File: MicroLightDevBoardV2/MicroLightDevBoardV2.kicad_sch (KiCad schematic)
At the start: 34 parts, among them J1 Conn_01x05_Socket, J10 TYPE-C-31-M-12, J11 Conn_01x04_Socket, J12 Conn_01x04_Socket, J2 Conn_01x05_Socket, J3 Conn_01x05_Socket, J4 Conn_01x05_Socket, J5 Conn_01x03_Socket, J6 Conn_01x04_Socket, J7 Conn_01x04_Socket, J8 Conn_01x05_Socket, J9 Conn_01x01_Socket, U1 BQ25628RYKR, U2 ATtiny3226-M, U3 USBLC6-2P6

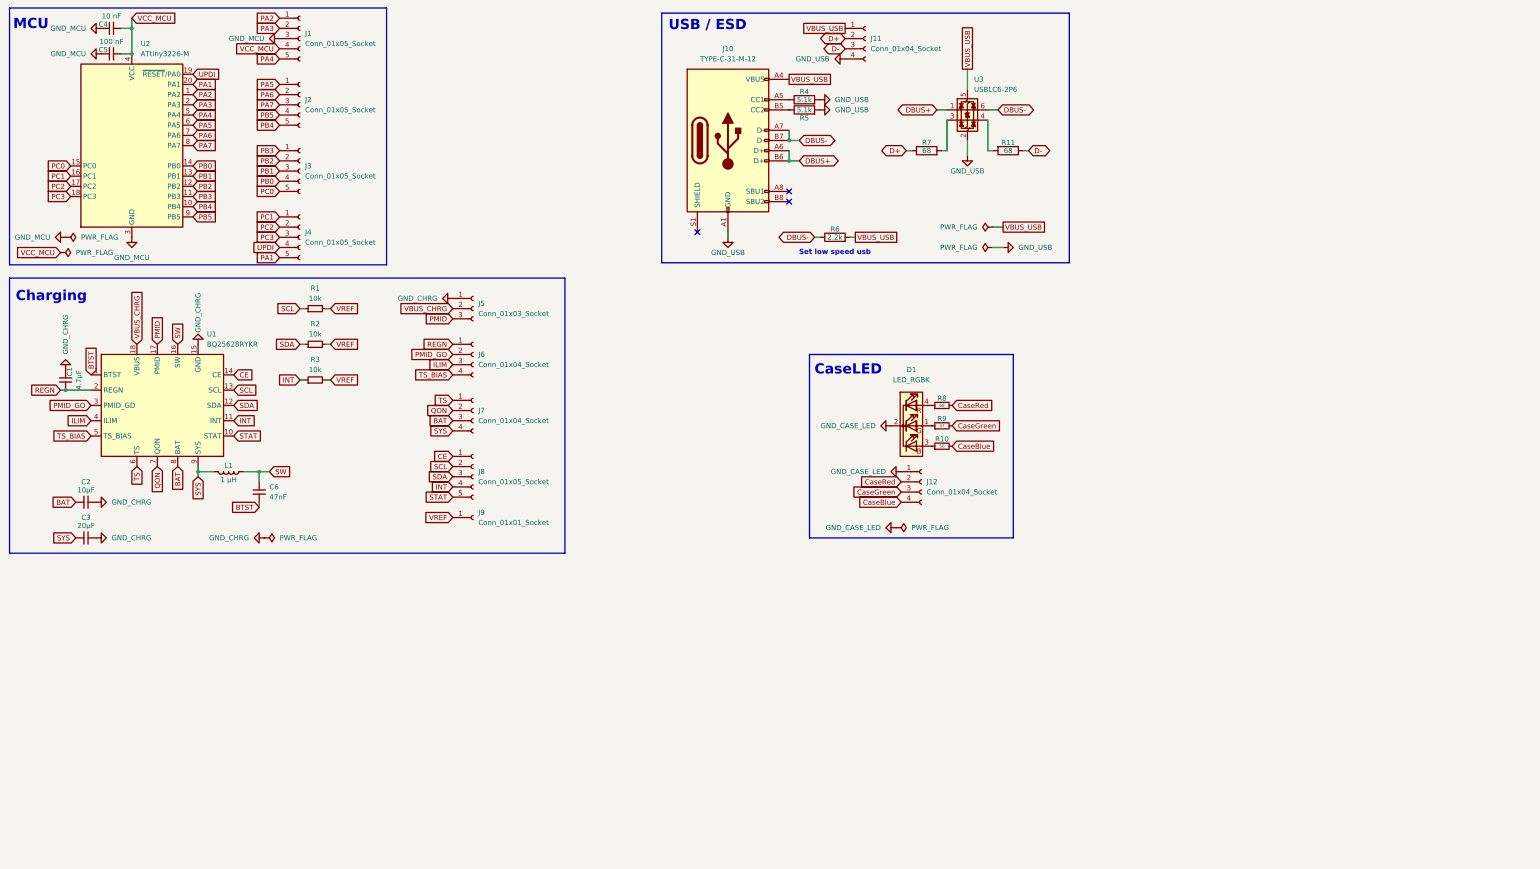
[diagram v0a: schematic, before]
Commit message: added symbol for accelerometer
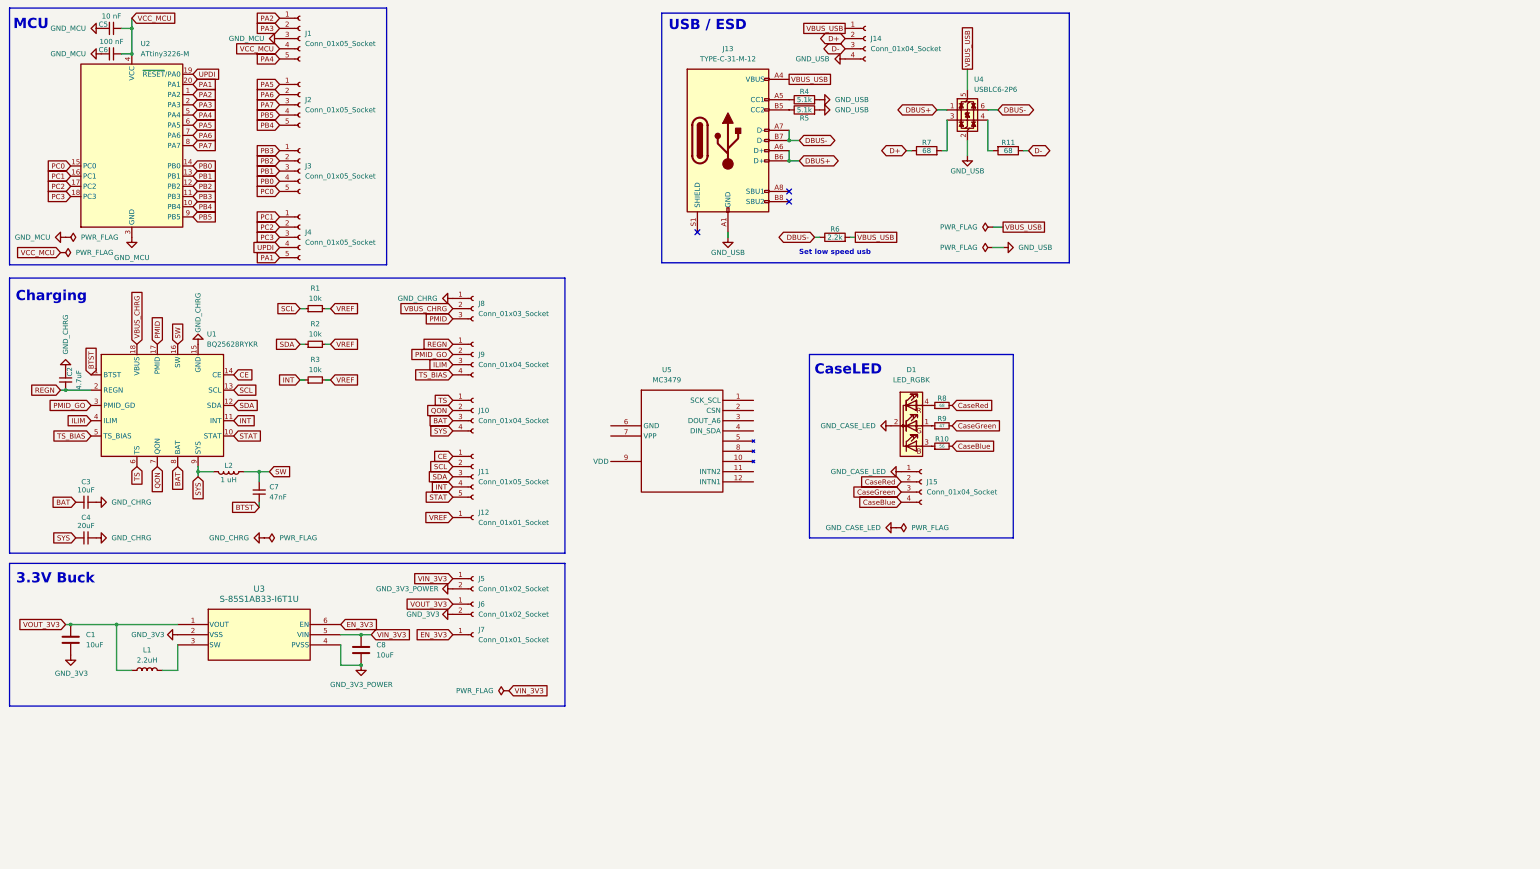
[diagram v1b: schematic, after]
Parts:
- added C1, C8: 10uF, symbol Device:C
- added J5, J6: Conn_01x02_Socket, symbol Connector:Conn_01x02_Socket
- added J7: Conn_01x01_Socket, symbol Connector:Conn_01x01_Socket
- added L1: 2.2uH, symbol Device:L
- added U3: S-85S1AB33-I6T1U, MicroLightDevBoard:SNT-6A-A-PKG_PG006-A-P-SD-2.1_ABL, symbol MicroLightDevBoard:S-85S1AB33-I6T1U
- added U5: MC3479, Package_LGA:LGA-12_2x2mm_P0.5mm, symbol MicroLightDevBoard:MC3479
- C2: renamed from C1; value 4.7μF -> 4.7uF
- C3: renamed from C2; value 10μF -> 10uF
- C4: renamed from C3; value 20μF -> 20uF
- L2: renamed from L1; value 1 μH -> 1 uH
- renumbered C4 to C5, C5 to C6, C6 to C7, J7 to J10, J8 to J11, J9 to J12, J10 to J13, J11 to J14, J12 to J15, J5 to J8, J6 to J9, U3 to U4
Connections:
- new net: L1.2, U3.3 (SW)
- new net EN_3V3: J7.1 (Pin_1), U3.6 (EN)
- new net GND_3V3: C1.2, J6.2 (Pin_2), U3.2 (VSS)
- new net GND_3V3_POWER: C8.2, J5.2 (Pin_2), U3.4 (PVSS)
- new net VIN_3V3: C8.1, J5.1 (Pin_1), U3.5 (VIN)
- new net VOUT_3V3: C1.1, J6.1 (Pin_1), L1.1, U3.1 (VOUT)
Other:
- note added: "3.3V Buck"

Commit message: added optional i2c though hole resister connectors in case I need to adjust, cleanup
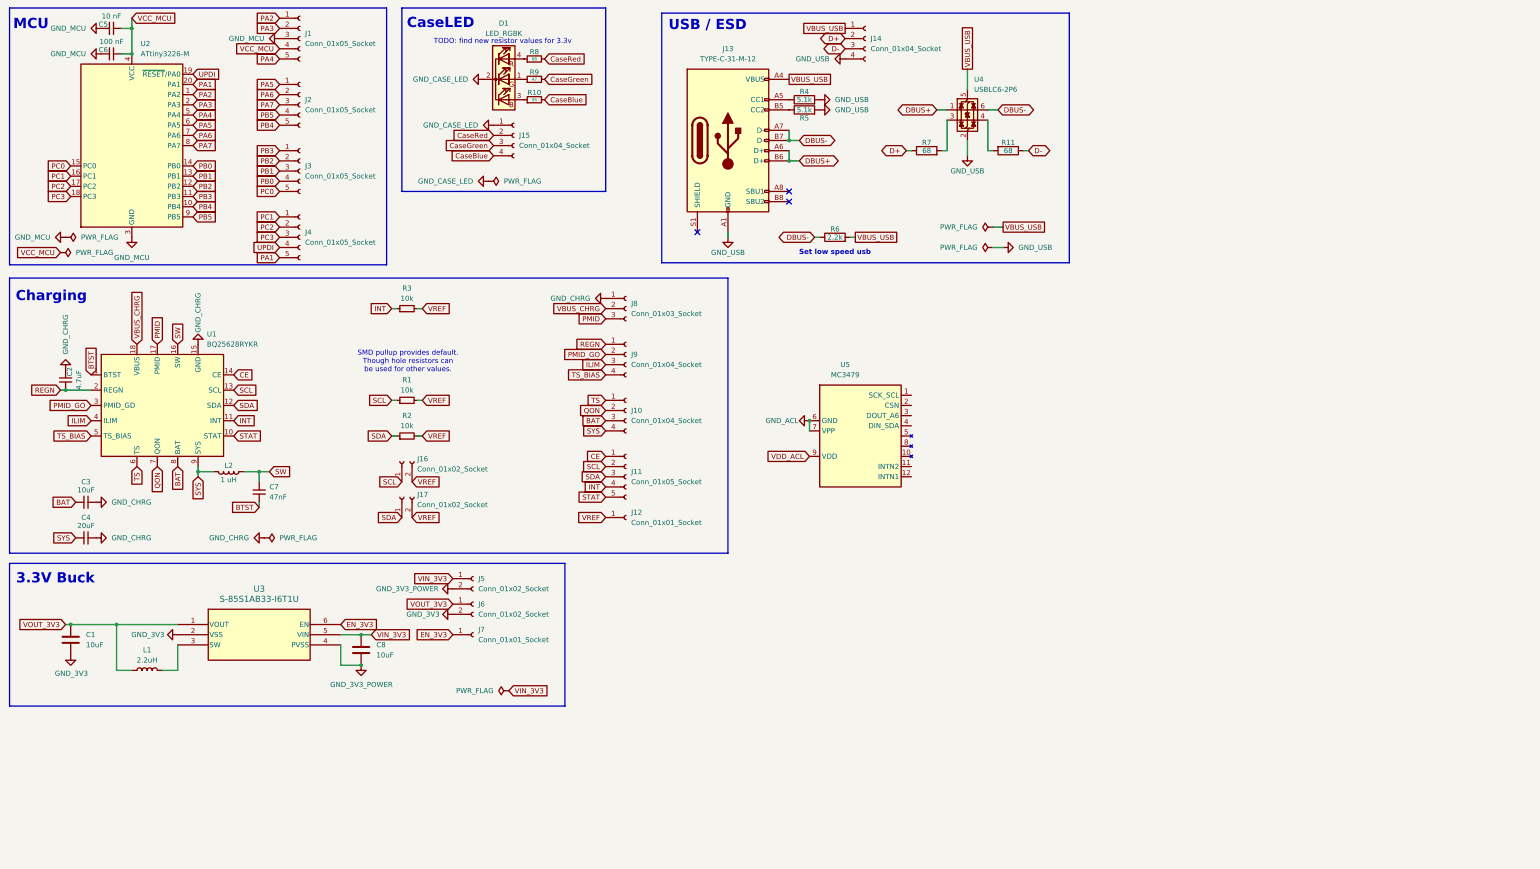
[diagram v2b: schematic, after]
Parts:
- added J16, J17: Conn_01x02_Socket, symbol Connector:Conn_01x02_Socket
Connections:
- net SCL: now also J16.1 (Pin_1)
- net SDA: now also J17.1 (Pin_1)
- net VREF: now also J16.2 (Pin_2), J17.2 (Pin_2)
- net GND_ACL: now reaches U5.6 (GND)
- net GND_ACL: now also U5.7 (VPP)
- net VDD_ACL: now reaches U5.9 (VDD)
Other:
- note added: "SMD pullup provides default. Though hole resistors can be used for other values."
- note added: "TODO: find new resistor values for 3.3v"
- moved on the sheet: D1, J10, J11, J12, J15, J8, J9, R1, R10, R2, R3, R8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

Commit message: Added accelerometer setup, should be compatible with i2c or spi
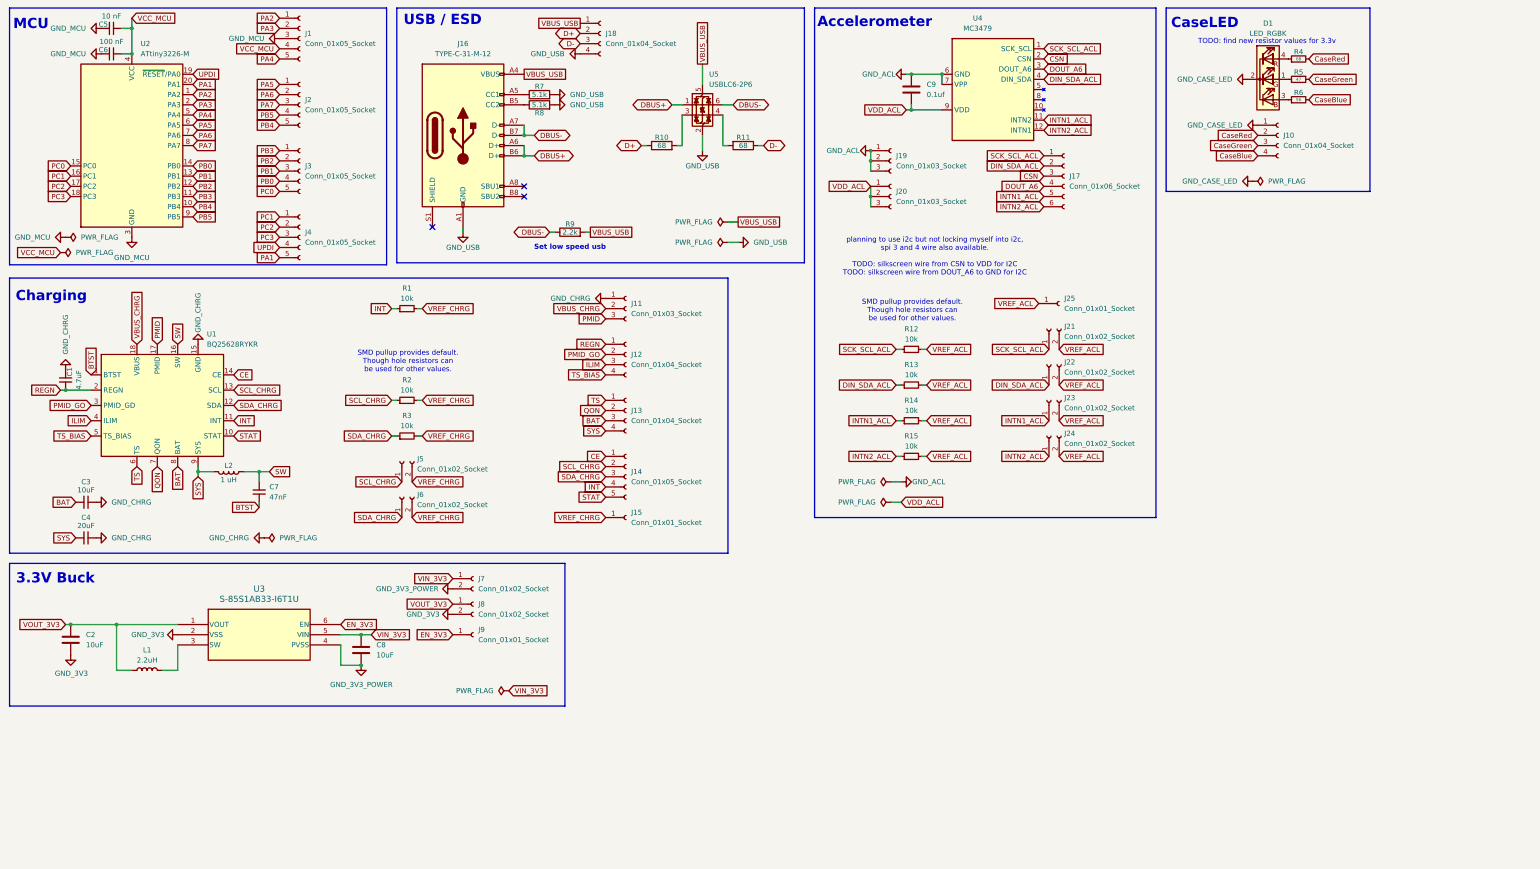
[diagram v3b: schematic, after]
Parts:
- added C9: 0.1uf, symbol Device:C
- added J17: Conn_01x06_Socket, symbol Connector:Conn_01x06_Socket
- added J19, J20: Conn_01x03_Socket, symbol Connector:Conn_01x03_Socket
- added J21, J22, J23, J24: Conn_01x02_Socket, symbol Connector:Conn_01x02_Socket
- added J25: Conn_01x01_Socket, symbol Connector:Conn_01x01_Socket
- added R12, R13, R14, R15: 10k, Resistor_SMD:R_0603_1608Metric, symbol Device:R_Small
- renumbered C2 to C1, C1 to C2, J15 to J10, J8 to J11, J9 to J12, J10 to J13, J11 to J14, J12 to J15, J13 to J16, J14 to J18, J16 to J5, J17 to J6, J5 to J7, J6 to J8, J7 to J9, R3 to R1, R7 to R10, R1 to R2, R2 to R3, R8 to R4, R9 to R5, R10 to R6, R4 to R7, R5 to R8, R6 to R9, U5 to U4, U4 to U5
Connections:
- net GND_ACL: now also C9.1, J19.1 (Pin_1), J19.2 (Pin_2), J19.3 (Pin_3)
- net VDD_ACL: now also C9.2, J20.1 (Pin_1), J20.2 (Pin_2), J20.3 (Pin_3)
- net SCK_SCL_ACL: now reaches U4.1 (SCK_SCL)
- net SCK_SCL_ACL: now also J17.1 (Pin_1), J21.1 (Pin_1), R12.1
- net INTN1_ACL: now reaches U4.11 (INTN2)
- net INTN1_ACL: now also J17.5 (Pin_5), J23.1 (Pin_1), R14.1
- net INTN2_ACL: now reaches U4.12 (INTN1)
- net INTN2_ACL: now also J17.6 (Pin_6), J24.1 (Pin_1), R15.1
- net CSN: now reaches U4.2 (CSN)
- net CSN: now also J17.3 (Pin_3)
- net DOUT_A6: now reaches U4.3 (DOUT_A6)
- net DOUT_A6: now also J17.4 (Pin_4)
- net DIN_SDA_ACL: now reaches U4.4 (DIN_SDA)
- net DIN_SDA_ACL: now also J17.2 (Pin_2), J22.1 (Pin_1), R13.1
- net SCL renamed SCL_CHRG
- net SDA renamed SDA_CHRG
- net VREF renamed VREF_CHRG
- new net VREF_ACL: J21.2 (Pin_2), J22.2 (Pin_2), J23.2 (Pin_2), J24.2 (Pin_2), J25.1 (Pin_1), R12.2, R13.2, R14.2, R15.2
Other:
- note added: "Accelerometer"
- note added: "planning to use i2c but not locking myself into i2c, spi 3 and 4 wire also available. TODO: silkscreen wire from CSN to VDD for I2C TODO: silkscreen wire from DOUT_A6 to GND for I2C"
- moved on the sheet: D1, J10, J16, J18, R10, R11, R4, R5, R6, R7, R8, R9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

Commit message: fixed symbols referencing old footprints and assigned footprints to rest
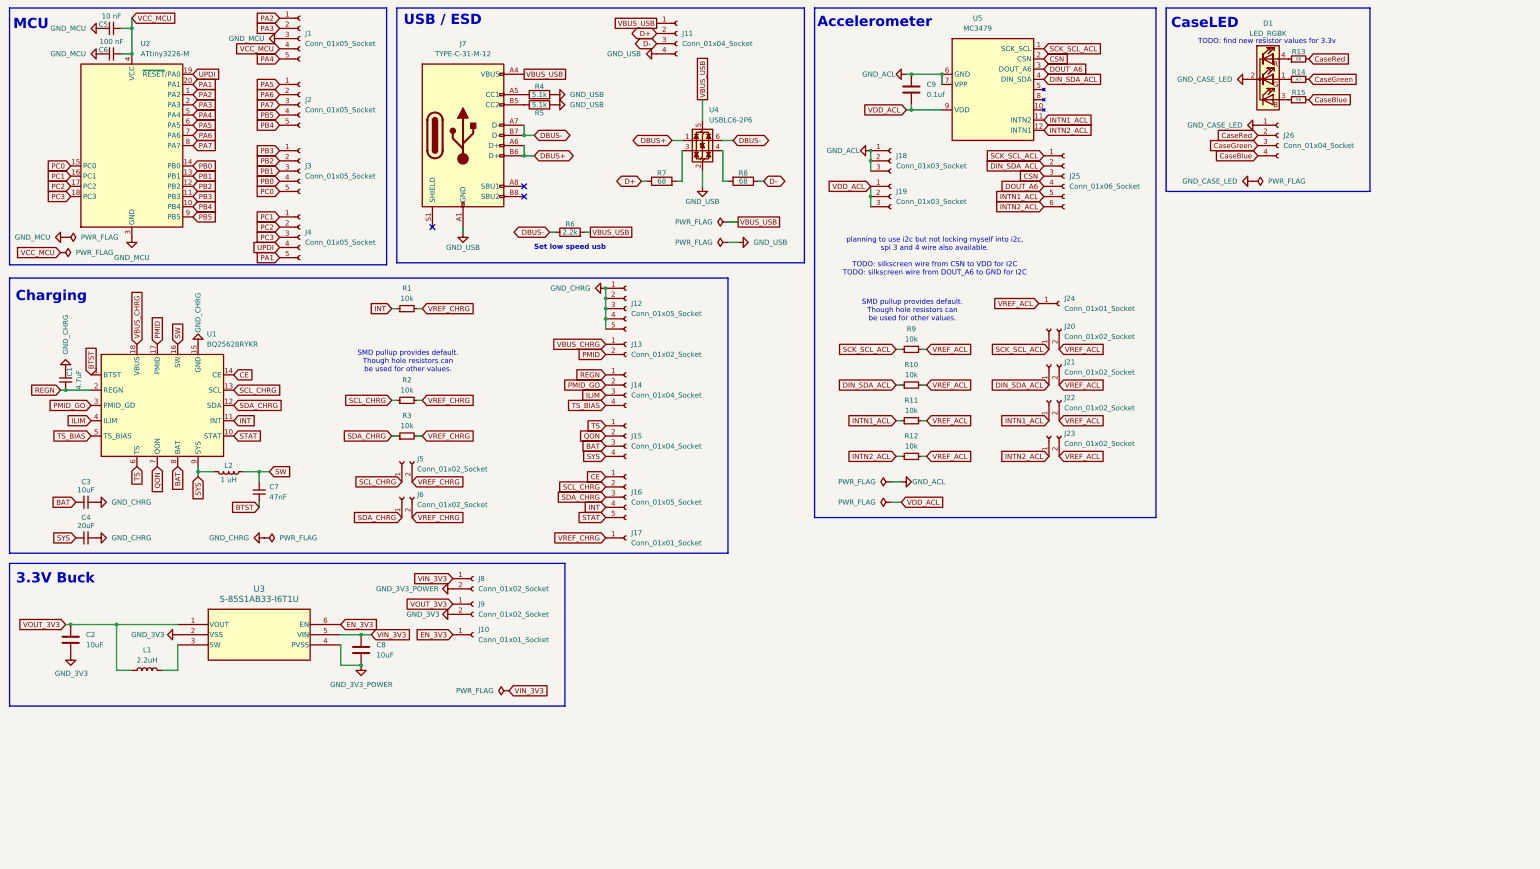
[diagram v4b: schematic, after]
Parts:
- removed J11: Conn_01x03_Socket, symbol Connector:Conn_01x03_Socket
- added J12: Conn_01x05_Socket, Connector_PinHeader_2.54mm:PinHeader_1x05_P2.54mm_Vertical, symbol Connector:Conn_01x05_Socket
- added J13: Conn_01x02_Socket, Connector_PinHeader_2.54mm:PinHeader_1x02_P2.54mm_Vertical, symbol Connector:Conn_01x02_Socket
- C2, C8, C9: footprint (none) -> Capacitor_SMD:C_0603_1608Metric
- D1: footprint BatteryExperimentPCB:RS-C1415MBAR -> MicroLightDevBoard:RS-C1415MBAR
- J1, J2, J3, J4: footprint (none) -> Connector_PinHeader_2.54mm:PinHeader_1x05_P2.54mm_Vertical
- J10: renamed from J9; footprint (none) -> Connector_PinHeader_2.54mm:PinHeader_1x01_P2.54mm_Vertical
- J11: renamed from J18; footprint (none) -> Connector_PinHeader_2.54mm:PinHeader_1x04_P2.54mm_Vertical
- J14: renamed from J12; footprint (none) -> Connector_PinHeader_2.54mm:PinHeader_1x04_P2.54mm_Vertical
- J15: renamed from J13; footprint (none) -> Connector_PinHeader_2.54mm:PinHeader_1x04_P2.54mm_Vertical
- J16: renamed from J14; footprint (none) -> Connector_PinHeader_2.54mm:PinHeader_1x05_P2.54mm_Vertical
- J17: renamed from J15; footprint (none) -> Connector_PinHeader_2.54mm:PinHeader_1x01_P2.54mm_Vertical
- J18: renamed from J19; footprint (none) -> Connector_PinHeader_2.54mm:PinHeader_1x03_P2.54mm_Vertical
- J19: renamed from J20; footprint (none) -> Connector_PinHeader_2.54mm:PinHeader_1x03_P2.54mm_Vertical
- J20: renamed from J21; footprint (none) -> Connector_PinHeader_2.54mm:PinHeader_1x02_P2.54mm_Vertical
- J21: renamed from J22; footprint (none) -> Connector_PinHeader_2.54mm:PinHeader_1x02_P2.54mm_Vertical
- J22: renamed from J23; footprint (none) -> Connector_PinHeader_2.54mm:PinHeader_1x02_P2.54mm_Vertical
- J23: renamed from J24; footprint (none) -> Connector_PinHeader_2.54mm:PinHeader_1x02_P2.54mm_Vertical
- J24: renamed from J25; footprint (none) -> Connector_PinHeader_2.54mm:PinHeader_1x01_P2.54mm_Vertical
- J25: renamed from J17; footprint (none) -> Connector_PinHeader_2.54mm:PinHeader_1x06_P2.54mm_Vertical
- J26: renamed from J10; footprint (none) -> Connector_PinHeader_2.54mm:PinHeader_1x04_P2.54mm_Vertical
- J5, J6: footprint (none) -> Connector_PinHeader_2.54mm:PinHeader_1x02_P2.54mm_Vertical
- J7: renamed from J16; footprint BatteryExperimentPCB:USB_C_Receptacle_Hroparts_TYPE-C-31-M-12 -> MicroLightDevBoard:USB_C_Receptacle_Hroparts_TYPE-C-31-M-12
- J8: renamed from J7; footprint (none) -> Connector_PinHeader_2.54mm:PinHeader_1x02_P2.54mm_Vertical
- J9: renamed from J8; footprint (none) -> Connector_PinHeader_2.54mm:PinHeader_1x02_P2.54mm_Vertical
- L1: footprint (none) -> Inductor_SMD:L_0805_2012Metric
- U1: footprint BatteryExperimentPCB:RYK0018A-MFG -> MicroLightDevBoard:RYK0018A-MFG
- renumbered R13 to R10, R14 to R11, R15 to R12, R4 to R13, R5 to R14, R6 to R15, R7 to R4, R8 to R5, R9 to R6, R10 to R7, R11 to R8, R12 to R9, U5 to U4, U4 to U5
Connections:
- net GND_CHRG: now also J12.1 (Pin_1), J12.2 (Pin_2), J12.3 (Pin_3), J12.4 (Pin_4), J12.5 (Pin_5)
- net PMID: now also J13.2 (Pin_2)
- net VBUS_CHRG: now also J13.1 (Pin_1)
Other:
- moved on the sheet: J11, J14, J15, J16, J17, R7, R8, U4
